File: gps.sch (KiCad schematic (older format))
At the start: 5 parts

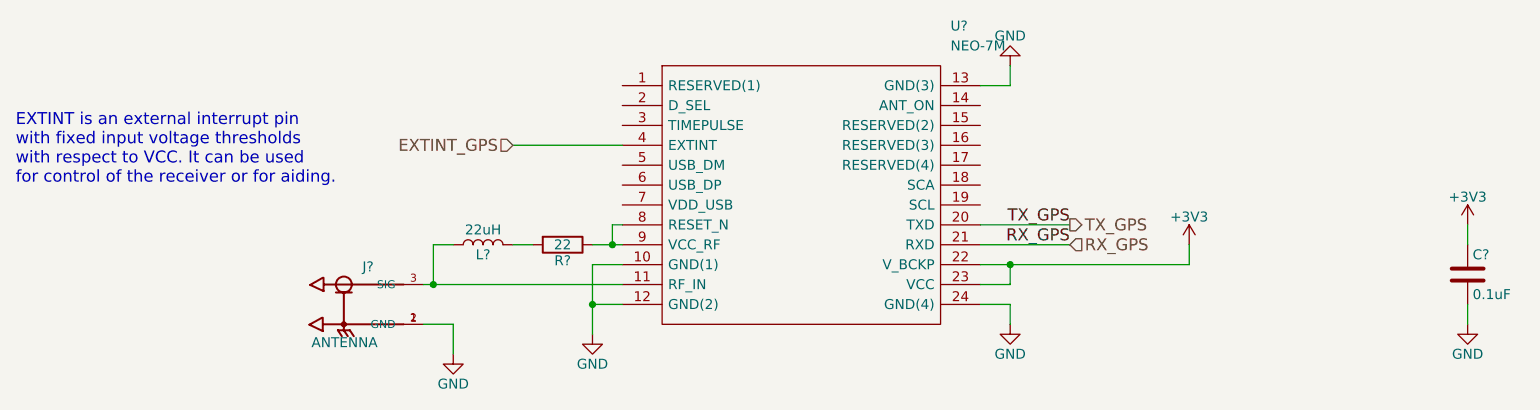
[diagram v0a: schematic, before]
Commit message: Improve battery as power source
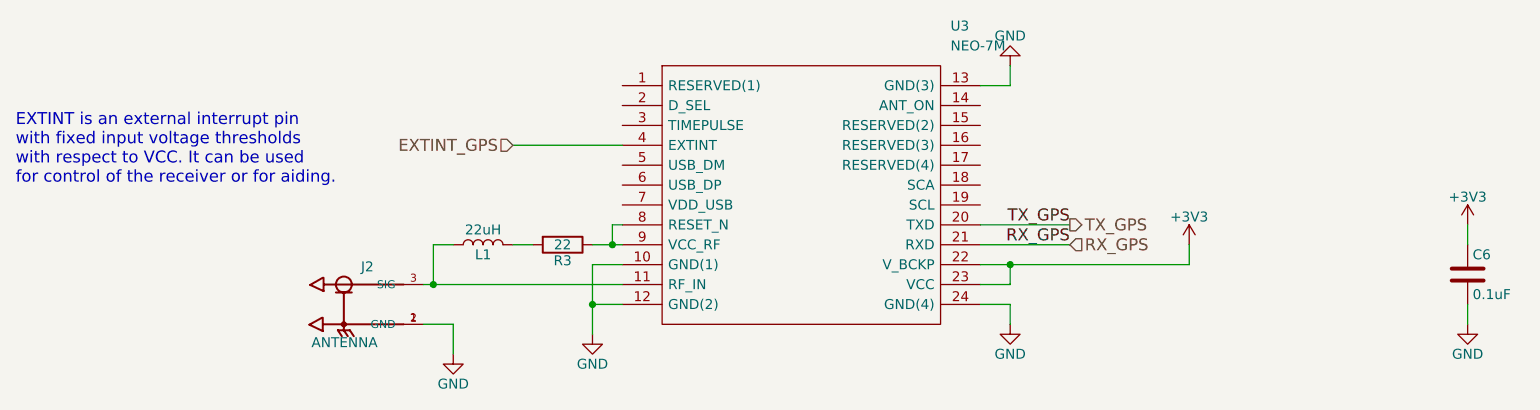
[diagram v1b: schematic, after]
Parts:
- gave numbers to parts that had none: 5
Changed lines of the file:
@@
 $EndDescr
 $Comp
-L NEO-7M U?
+L NEO-7M U3
 U 1 1 5A86191F
 P 5050 3100
-F 0 "U?" H 6700 3400 50  0000 L CNN
+F 0 "U3" H 6700 3400 50  0000 L CNN
 F 1 "NEO-7M" H 6700 3300 50  0000 L CNN
 F 2 "NEO-7M" H 6700 3200 50  0001 L CNN
@@
 	4900 4000 4900 4350
 $Comp
-L GND #PWR?
+L GND #PWR013
 U 1 1 5A861DFB
 P 4900 4350
-F 0 "#PWR?" H 4900 4100 50  0001 C CNN
+F 0 "#PWR013" H 4900 4100 50  0001 C CNN
 F 1 "GND" H 4900 4200 50  0000 C CNN
 F 2 "" H 4900 4350 50  0001 C CNN
@@
 	7000 4200 7000 4300
 $Comp
-L GND #PWR?
+L GND #PWR014
 U 1 1 5A861E30
 P 7000 4300
-F 0 "#PWR?" H 7000 4050 50  0001 C CNN
+F 0 "#PWR014" H 7000 4050 50  0001 C CNN
 F 1 "GND" H 7000 4150 50  0000 C CNN
 F 2 "" H 7000 4300 50  0001 C CNN
@@
 	7000 3100 7000 3000
 $Comp
-L GND #PWR?
+L GND #PWR015
 U 1 1 5A861E6C
 P 7000 3000
-F 0 "#PWR?" H 7000 2750 50  0001 C CNN
+F 0 "#PWR015" H 7000 2750 50  0001 C CNN
 F 1 "GND" H 7000 2850 50  0000 C CNN
 F 2 "" H 7000 3000 50  0001 C CNN
@@
 $EndComp
 $Comp
-L U.FL-R-SMT(01) J?
+L U.FL-R-SMT(01) J2
 U 1 1 5A861F80
 P 3650 4200
-F 0 "J?" H 3500 4360 50  0000 L BNN
+F 0 "J2" H 3500 4360 50  0000 L BNN
 F 1 "ANTENNA" H 3480 3979 50  0000 L BNN
 F 2 "HRS_U.FL-R-SMT(01)" H 3650 4200 50  0001 L BNN
@@
 	4200 4300 4200 4450
 $Comp
-L GND #PWR?
+L GND #PWR016
 U 1 1 5A862015
 P 4200 4450
-F 0 "#PWR?" H 4200 4200 50  0001 C CNN
+F 0 "#PWR016" H 4200 4200 50  0001 C CNN
 F 1 "GND" H 4200 4300 50  0000 C CNN
 F 2 "" H 4200 4450 50  0001 C CNN
@@
 	7900 4000 7900 3900
 $Comp
-L +3V3 #PWR?
+L +3V3 #PWR017
 U 1 1 5A86222C
 P 7900 3900
-F 0 "#PWR?" H 7900 3750 50  0001 C CNN
+F 0 "#PWR017" H 7900 3750 50  0001 C CNN
 F 1 "+3V3" H 7900 4040 50  0000 C CNN
 F 2 "" H 7900 3900 50  0001 C CNN
@@
 	5050 3900 4900 3900
 $Comp
-L R R?
+L R R3
 U 1 1 5A8624A2
 P 4750 3900
-F 0 "R?" V 4830 3900 50  0000 C CNN
+F 0 "R3" V 4830 3900 50  0000 C CNN
 F 1 "22" V 4750 3900 50  0000 C CNN
 F 2 "" V 4680 3900 50  0001 C CNN
@@
 	4600 3900 4500 3900
 $Comp
-L L L?
+L L L1
 U 1 1 5A8624DF
 P 4350 3900
-F 0 "L?" V 4300 3900 50  0000 C CNN
+F 0 "L1" V 4300 3900 50  0000 C CNN
 F 1 "22uH" V 4425 3900 50  0000 C CNN
 F 2 "" H 4350 3900 50  0001 C CNN
@@
 Connection ~ 7000 4000
 $Comp
-L C C?
+L C C6
 U 1 1 5A862F84
 P 9300 4050
-F 0 "C?" H 9325 4150 50  0000 L CNN
+F 0 "C6" H 9325 4150 50  0000 L CNN
 F 1 "0.1uF" H 9325 3950 50  0000 L CNN
 F 2 "" H 9338 3900 50  0001 C CNN
@@
 	9300 3900 9300 3800
 $Comp
-L +3V3 #PWR?
+L +3V3 #PWR018
 U 1 1 5A862FF9
 P 9300 3800
-F 0 "#PWR?" H 9300 3650 50  0001 C CNN
+F 0 "#PWR018" H 9300 3650 50  0001 C CNN
 F 1 "+3V3" H 9300 3940 50  0000 C CNN
 F 2 "" H 9300 3800 50  0001 C CNN
@@
 	9300 4200 9300 4300
 $Comp
-L GND #PWR?
+L GND #PWR019
 U 1 1 5A863045
 P 9300 4300
-F 0 "#PWR?" H 9300 4050 50  0001 C CNN
+F 0 "#PWR019" H 9300 4050 50  0001 C CNN
 F 1 "GND" H 9300 4150 50  0000 C CNN
 F 2 "" H 9300 4300 50  0001 C CNN
